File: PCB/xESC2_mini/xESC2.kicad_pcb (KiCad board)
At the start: 4 copper layers, 49.5 x 29 mm, 108 parts, among them J1 Conn_01x06_Male, J10 Conn_01x06_Male, J2 U254-051T-4BH83-F1S, J3 Conn_01x05_Male, J4 Conn_01x05_Male, J5 Conn_01x03_Male, J6 Conn_02x02_Counter_Clockwise, J7 Conn_02x02_Counter_Clockwise, J8 Conn_02x02_Counter_Clockwise, J9 Conn_01x06_Male, Q1 BSC026N08NS5, Q2 BSC026N08NS5, Q3 BSC026N08NS5, Q4 BSC026N08NS5, Q5 BSC026N08NS5, Q6 BSC026N08NS5, U1 TMC6200-TA, U2 XC6220B331MR, U4 STM32F405RGTx, U5 SN65HVD232, Y1 Crystal_GND24

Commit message: added fiducials
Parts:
- added FID1: Fiducial, Fiducial:Fiducial_0.75mm_Mask1.5mm, F.Cu at (275.5, 129.4)
- added FID2: Fiducial, Fiducial:Fiducial_0.75mm_Mask1.5mm, F.Cu at (275.5, 107.4)
- added FID3: Fiducial, Fiducial:Fiducial_0.75mm_Mask1.5mm, F.Cu at (234.9, 129.8)
- added FID4: Fiducial, Fiducial:Fiducial_0.75mm_Mask1.5mm, B.Cu at (275.5, 129.4)
- added FID5: Fiducial, Fiducial:Fiducial_0.75mm_Mask1.5mm, F.Cu at (232.8, 107.3)
- added FID6: Fiducial, Fiducial:Fiducial_0.75mm_Mask1.5mm, B.Cu at (231.4, 124.8)
- added FID7: Fiducial, Fiducial:Fiducial_0.75mm_Mask1.5mm, B.Cu at (275.5, 107.4)
- added FID8: Fiducial, Fiducial:Fiducial_0.75mm_Mask1.5mm, B.Cu at (232.8, 107.3)
- R14, R15: value DNP -> 10k

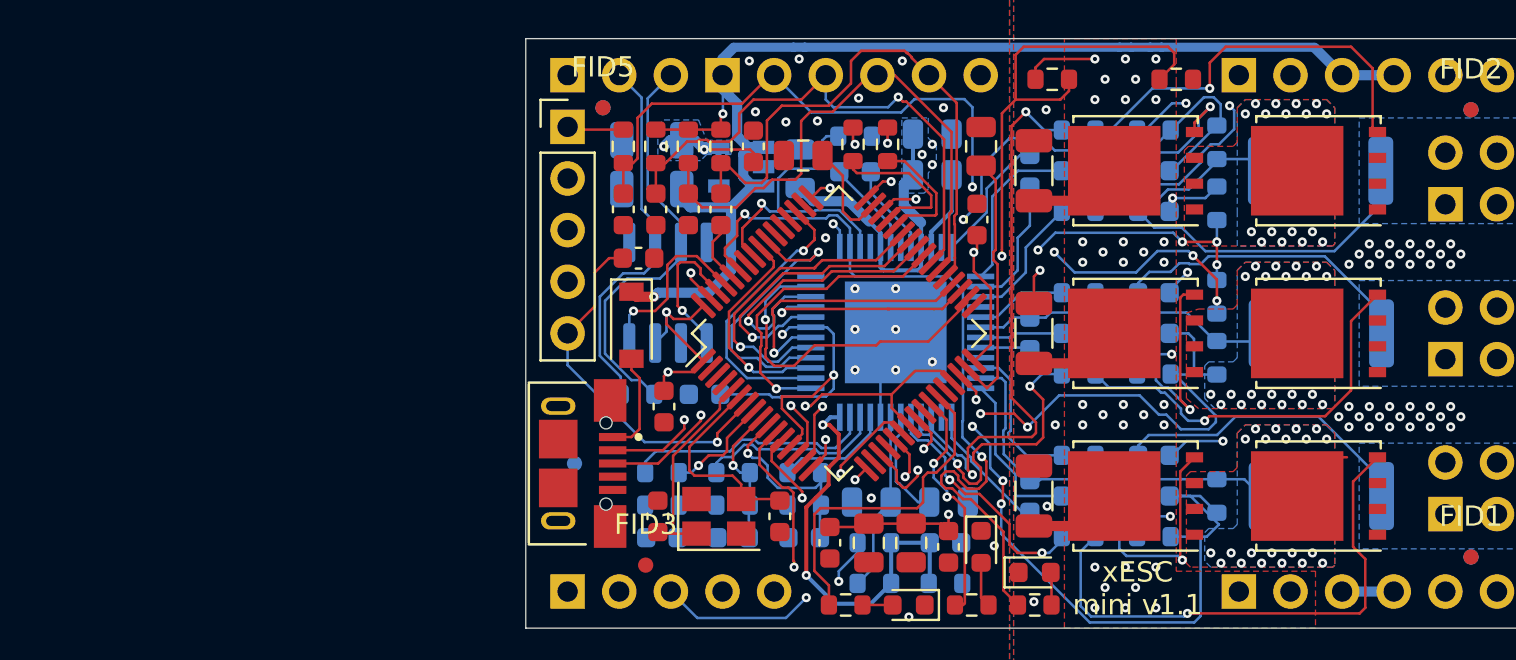
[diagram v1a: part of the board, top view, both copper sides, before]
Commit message: wip - had not save the pcb with tmp footprint inserted to check routing
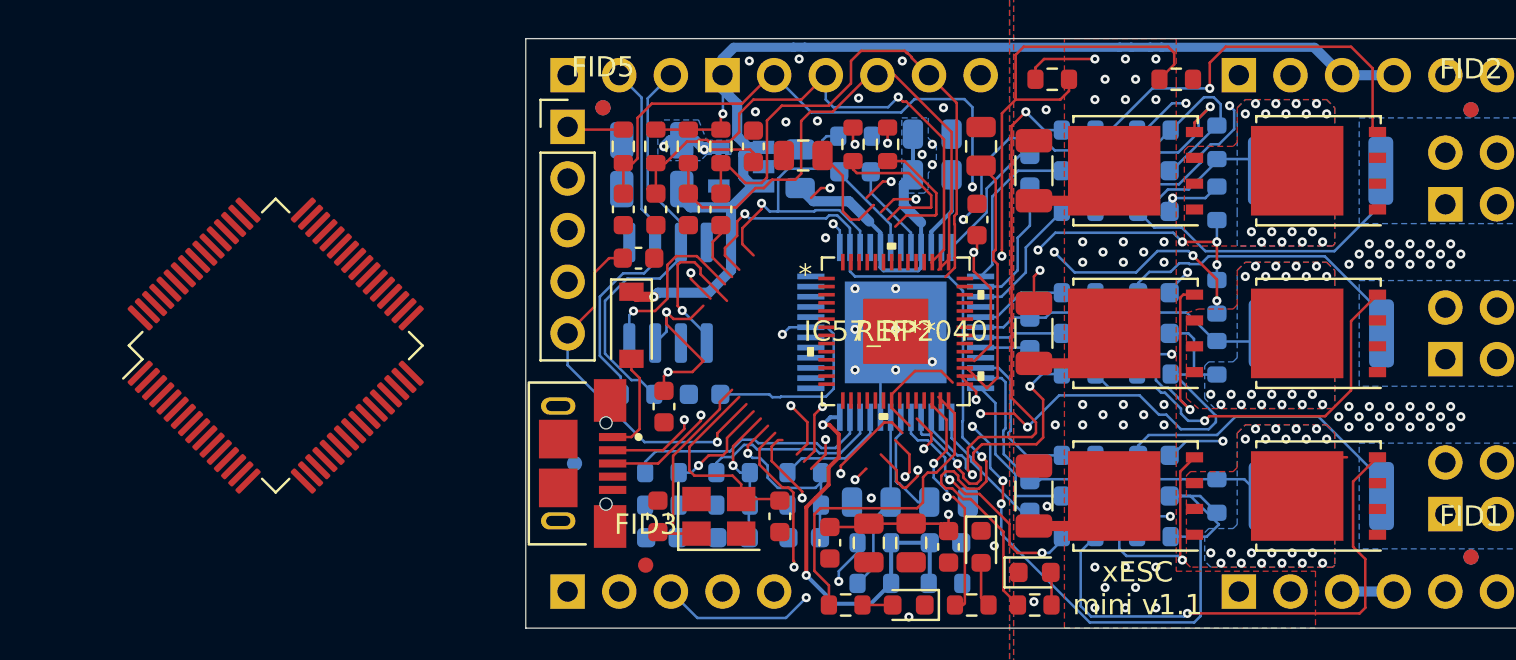
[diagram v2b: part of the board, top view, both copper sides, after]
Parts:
- added REF**: IC57_RP2040, xESC2:RP2040, F.Cu at (247.2, 118.3)
- moved U4 27.7 mm to (216.7, 119.0)
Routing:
- net /MCU/WL: track 16.9 -> 0.00 mm, vias 1 -> 0
- net /MCU/UH: track 15.8 -> 0.00 mm, vias 1 -> 0
- net /MCU/DRV_NCS: track 15.2 -> 0.00 mm, vias 1 -> 0
- net /MCU/DRV_MISO: track 14.5 -> 0.00 mm, vias 1 -> 0
- net /MCU/VH: track 14.4 -> 0.00 mm, vias 1 -> 0
- net /MCU/WH: track 14.3 -> 0.00 mm, vias 1 -> 0
- net /MCU/DRV_SCK: track 14.1 -> 0.00 mm, vias 1 -> 0
- net /MCU/UL: track 13.7 -> 0.00 mm, vias 1 -> 0
- net /MCU/VL: track 10.8 -> 0.00 mm, vias 1 -> 0
- net /MCU/DRV_MOSI: track 10.7 -> 0.00 mm, vias 1 -> 0
- net +3V3: track 76.8 -> 70.6 mm, vias 15 -> 14
- net /MCU/TX_MOSI_EXT: track 23.2 -> 18.7 mm, vias 1 -> 0
- added copper zone on In2.Cu, net +3V3
- added copper zone on In2.Cu, net /VM
- added copper zone on In1.Cu, net GND
- removed copper zone on VM, net +3V3
- removed copper zone on VM, net /VM
- removed copper zone on GND, net GND
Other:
- net class Default removed

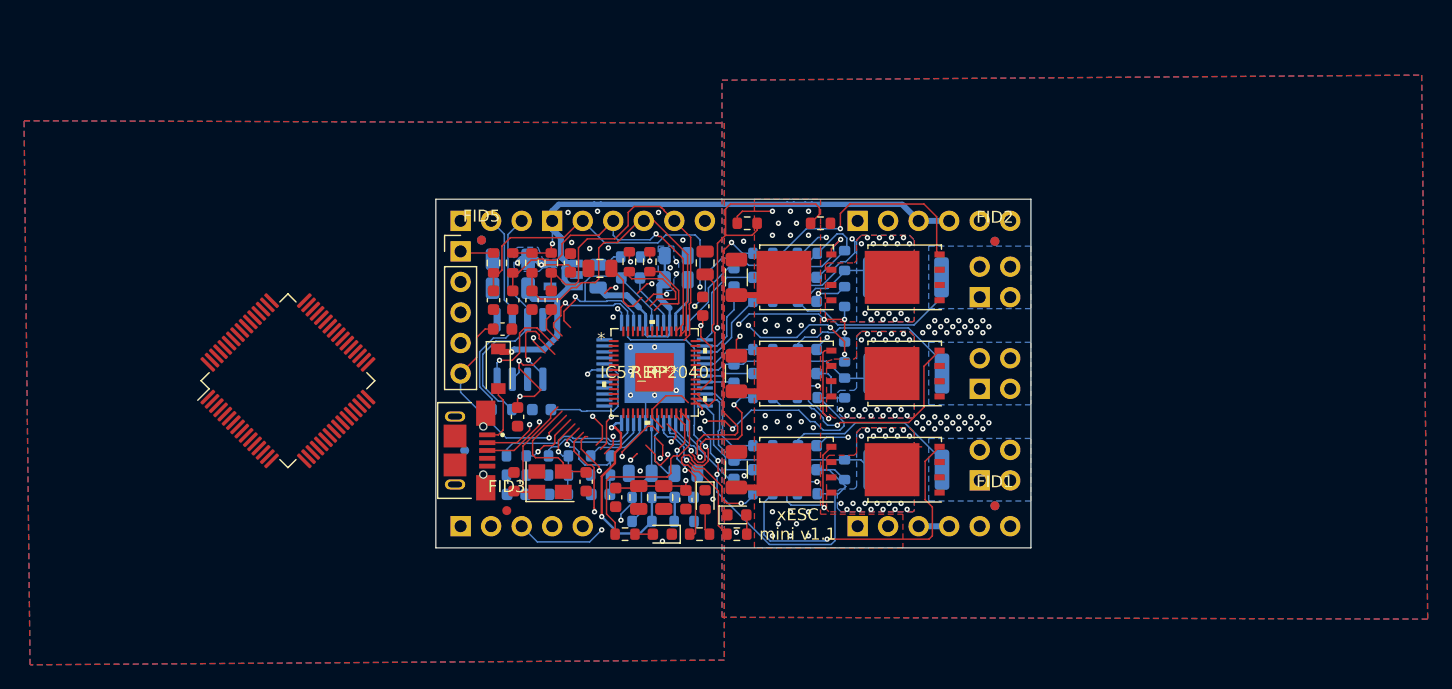
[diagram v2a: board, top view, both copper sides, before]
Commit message: wip - most routing for RP2040 done
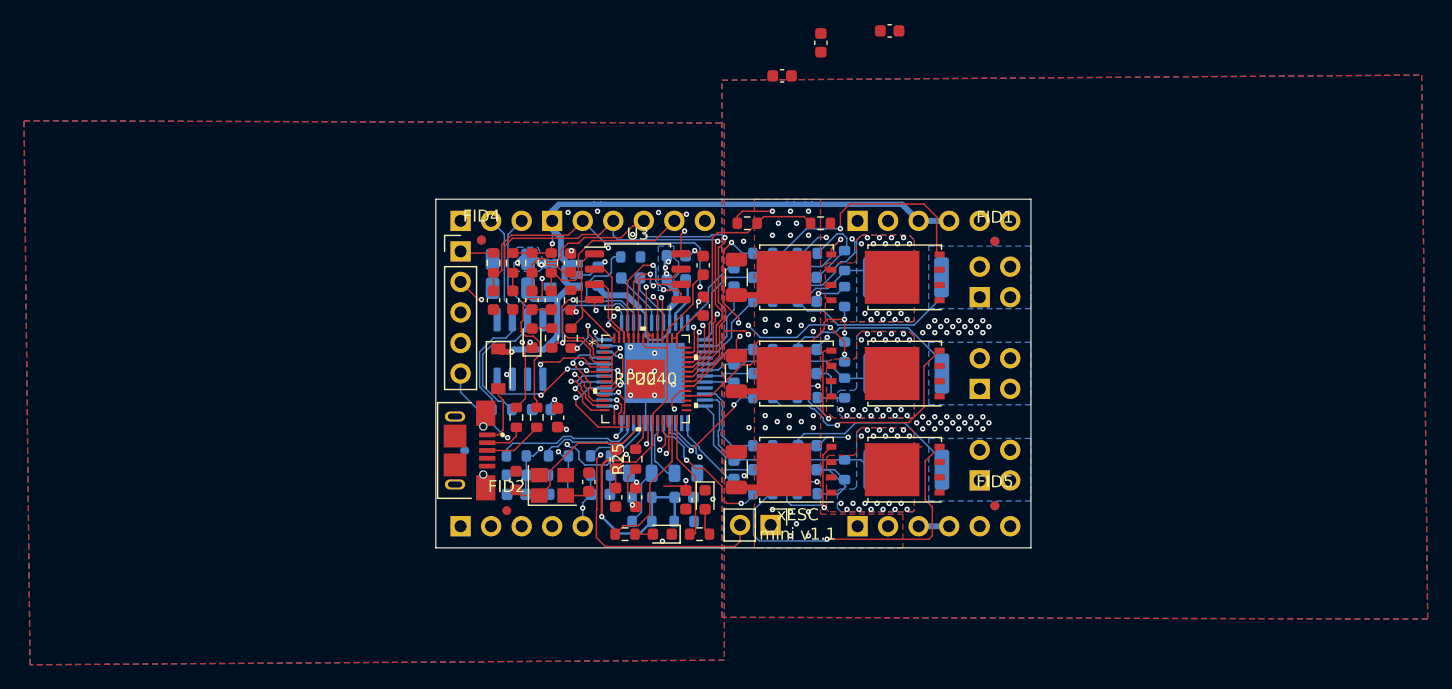
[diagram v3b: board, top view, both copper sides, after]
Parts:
- removed the C32 at (235.5, 127.4)
- removed the C33 at (241.5, 127.4)
- removed the C34 at (234.6, 114.7)
- removed the C35 at (251.4, 109.2)
- removed the C36 at (242.7, 109.7)
- removed the C38 at (248.0, 128.7)
- removed the C39 at (245.9, 128.7)
- removed REF**: IC57_RP2040, xESC2:RP2040
- removed the U4 at (216.7, 119.0)
- added C11: 27pF, Capacitor_SMD:C_0603_1608Metric, F.Cu at (235.7, 127.3)
- added C12: 27pF, Capacitor_SMD:C_0603_1608Metric, F.Cu at (241.7, 127.4)
- added C13: 1uF, Capacitor_SMD:C_0603_1608Metric, F.Cu at (266.8, 89.9)
- added C14: .1uF, Capacitor_SMD:C_0603_1608Metric, F.Cu at (257.8, 93.6)
- added C15: .1uF, Capacitor_SMD:C_0603_1608Metric, F.Cu at (245.6, 128.7)
- added C16: .1uF, Capacitor_SMD:C_0603_1608Metric, F.Cu at (239.1, 122.1)
- added C23: .1uF, Capacitor_SMD:C_0603_1608Metric, F.Cu at (244.0, 125.5)
- added C24: 1uF, Capacitor_SMD:C_0603_1608Metric, F.Cu at (251.2, 109.4)
- added J6: Conn_01x02, Connector_PinHeader_2.54mm:PinHeader_1x02_P2.54mm_Vertical, F.Cu at (256.9, 131.0)
- added R25: 1K, Resistor_SMD:R_0603_1608Metric, F.Cu at (245.6, 125.5)
- added R26: 1K, Resistor_SMD:R_0603_1608Metric, F.Cu at (240.2, 112.3)
- added R27: 10K, Resistor_SMD:R_0603_1608Metric, F.Cu at (240.2, 115.5)
- added U2: RP2040, xESC2:RP2040, F.Cu at (246.4, 118.8)
- added U3: W25Q128JVS, Package_SO:SOIC-8_5.23x5.23mm_P1.27mm, F.Cu at (245.8, 110.3)
- C17: renamed from C40; value 100nF/50V -> .1uF
- C18: renamed from C41; value 100nF/50V -> .1uF
- C19: renamed from C42; value 100nF/50V -> .1uF
- C2: renamed from C44; value 100nF/50V -> .1uF
- C20: renamed from C43; value 100nF/50V -> .1uF
- C22: renamed from C37; value 100nF/50V -> .1uF
- C29: renamed from C6; value 100nF/50V -> .1uF
- C30: renamed from C7; value 100nF/50V -> .1uF
- C32: renamed from C12; value 100nF/100V -> .1uF; footprint Capacitor_SMD:C_0805_2012Metric -> Capacitor_SMD:C_0603_1608Metric
- C33: renamed from C13; value 100nF/100V -> .1uF; footprint Capacitor_SMD:C_0805_2012Metric -> Capacitor_SMD:C_0603_1608Metric
- C34: renamed from C14; value 100nF/100V -> .1uF; footprint Capacitor_SMD:C_0805_2012Metric -> Capacitor_SMD:C_0603_1608Metric
- R22: renamed from R41; value 10k -> 10K
- R3: renamed from R30; value 10k -> 10K
- R32: renamed from R29; value 10k -> 10K
- R35: renamed from R14; value 10k -> 10K
- R36: renamed from R15; value 10k -> 10K
- Y1: value Crystal_GND24 -> Crystal
- moved C18 40.1 mm to (261.0, 90.9)
- moved D4 22.5 mm to (237.0, 115.5), turned to 90 degrees
- moved R33 22.4 mm to (238.7, 115.5), turned to 90 degrees
- moved R6 17.1 mm to (235.7, 122.0), turned to -90 degrees
- moved R7 15.1 mm to (237.4, 122.0), turned to -90 degrees
- moved Y1 0.36 mm to (238.7, 127.7)
- moved C17 0.05 mm to (251.2, 112.8)
- renumbered C15 to C1, C31 to C10, C1 to C25, C24 to C26, C4 to C27, C5 to C28, C45 to C3, C11 to C31, C8 to C35, C9 to C36, C10 to C37, C20 to C38, C21 to C39, C27 to C4, C2 to C40, C25 to C41, C3 to C42, C26 to C43, C46 to C5, C47 to C6, C28 to C7, C29 to C8, C30 to C9, D3 to D1, D4 to D2, D5 to D3, D2 to D4, FID2 to FID1, FID3 to FID2, FID4 to FID3, FID5 to FID4, FID1 to FID5, J7 to J10, J8 to J11, J6 to J7, J9 to J8, J10 to J9, R17 to R1, R21 to R10, R22 to R11, R35 to R12, R23 to R13, R24 to R14, R36 to R15, R25 to R16, R26 to R17, R27 to R18, R28 to R19, R18 to R2, R39 to R20, R40 to R21, R37 to R23, R38 to R24, R1 to R28, R2 to R29, R3 to R30, R4 to R31, R16 to R33, R13 to R34, R5 to R37, R6 to R38, R7 to R39, R19 to R4, R8 to R40, R9 to R41, R10 to R42, R11 to R43, R12 to R44, R20 to R5, R31 to R6, R32 to R7, R33 to R8, R34 to R9, U5 to U1, U1 to U4, U2 to U5
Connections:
- net /MCU/FAULT renamed /Power/FAULT
- C22 pad 1: +3V3 -> /MCU/1.1V
- J2 pad 4: (no net) -> unconnected-(J2-Pad4)
- J4 pad 1: /MCU/MISO_EXT -> /MISO_EXT
- J4 pad 2: /MCU/TX_MOSI_EXT -> /TX_MOSI_EXT
- J4 pad 3: /MCU/SCK_EXT -> /SCK_EXT
- J4 pad 4: /MCU/RX_NCS_EXT -> /RX_NCS_EXT
- U1 pad 5: (no net) -> unconnected-(U1-Pad5)
- U1 pad 8: (no net) -> unconnected-(U1-Pad8)
- U4 pad 2: (no net) -> unconnected-(U4-Pad2)
- U4 pad 28: (no net) -> unconnected-(U4-Pad28)
- U4 pad 31: (no net) -> unconnected-(U4-Pad31)
- U4 pad 35: (no net) -> unconnected-(U4-Pad35)
- U4 pad 40: (no net) -> unconnected-(U4-Pad40)
- U4 pad 45: (no net) -> unconnected-(U4-Pad45)
- U5 pad 4: (no net) -> unconnected-(U5-Pad4)
- Y1 pad 1: Net-(C32-Pad1) (its old number) -> /MCU/Xin
- Y1 pad 2: GND -> Net-(C12-Pad2)
- Y1 pad 3: Net-(C33-Pad1) -> (no net)
- Y1 pad 4: GND -> (no net)
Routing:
- net Net-(J6-Pad2): track 0.00 -> 43.2 mm, vias 0 -> 2
- net /V_M_FILTERED: track 52.9 -> 21.1 mm, vias 2 -> 0
- net /PHASE_U_FILTERED: track 39.1 -> 8.30 mm, vias 4 -> 0
- net /PHASE_W_FILTERED: track 36.9 -> 7.71 mm, vias 2 -> 0
- net /PHASE_V_FILTERED: track 33.1 -> 5.35 mm, vias 3 -> 0
- net Net-(J2-Pad3): track 30.1 -> 4.95 mm, vias 2 -> 0
- net /MCU/1.1V: track 0.00 -> 24.1 mm
- net /CUR_V: track 7.07 -> 31.0 mm, vias 1 -> 2
- net /CUR_U: track 10.2 -> 33.7 mm, vias 1 -> 2
- net Net-(J2-Pad2): track 26.8 -> 3.38 mm, vias 2 -> 0
- net /Power/FAULT: track 38.2 -> 15.3 mm, vias 2 -> 1
- net /MCU/MISO_EXT: track 22.8 -> 0.00 mm, vias 1 -> 0
- net /CUR_W: track 8.54 -> 31.1 mm, vias 1 -> 2
- net /USB_DM: track 6.38 -> 27.7 mm, vias 0 -> 2
- net /MCU/RX_NCS_EXT: track 20.9 -> 0.00 mm, vias 1 -> 0
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- added copper zone on B.Cu, net Net-(C31-Pad1)
- removed copper zone on B.Cu, net Net-(C26-Pad1)

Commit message: wip - clean up silkscreen layer add some 3d obj
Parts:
- U4: value TMC6200-TA -> eTQFP48_9x9_TRI
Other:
- board text added: "USB Boot"
- board text added: "xESC mini v1.2"
- board text removed: "xESC mini v1.1"

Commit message: wip - landed a couple more bypass caps - 2 left
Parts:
- moved C14 29.3 mm to (253.7, 122.7)
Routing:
- net +3V3: track 59.8 -> 64.4 mm, vias 18 -> 19
- net /Power/LSW: track 26.1 -> 28.6 mm, vias 3 -> 4
- net /Power/LSV: track 10.4 -> 12.6 mm
- net /MCU/SWDCLK: track 33.6 -> 31.4 mm
- net /PCB_TEMP: track 19.8 -> 21.4 mm, vias 2 -> 4
- net /Power/SENSE_U: track 7.58 -> 6.56 mm
- net /HALL3: track 44.6 -> 45.5 mm
- net GND: vias 71 -> 72
- net /MCU/SWDIO: vias 2 -> 3
